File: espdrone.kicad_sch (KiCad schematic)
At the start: 46 parts, among them U15 TPD2EUSB30A, U3 W25Q128JVP, U7 GT-USB-7079C, Y1 Crystal_GND24

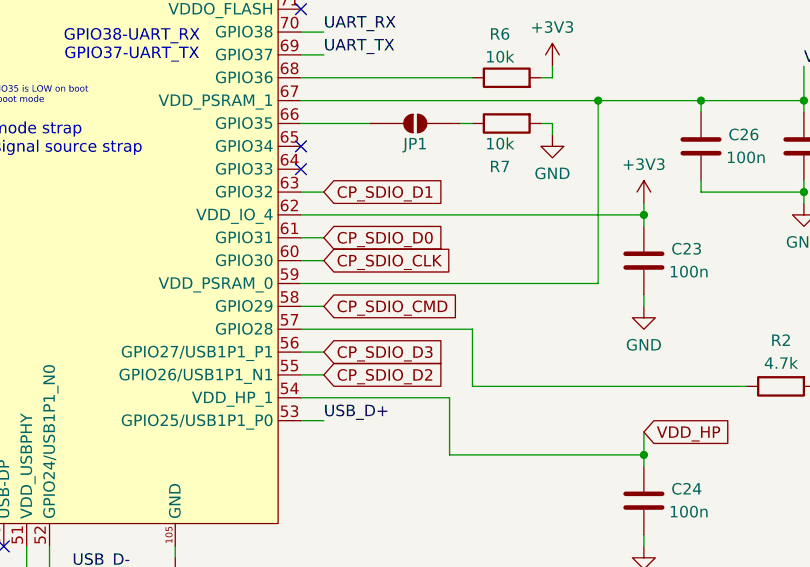
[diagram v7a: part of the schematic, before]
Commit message: Add some FC vias
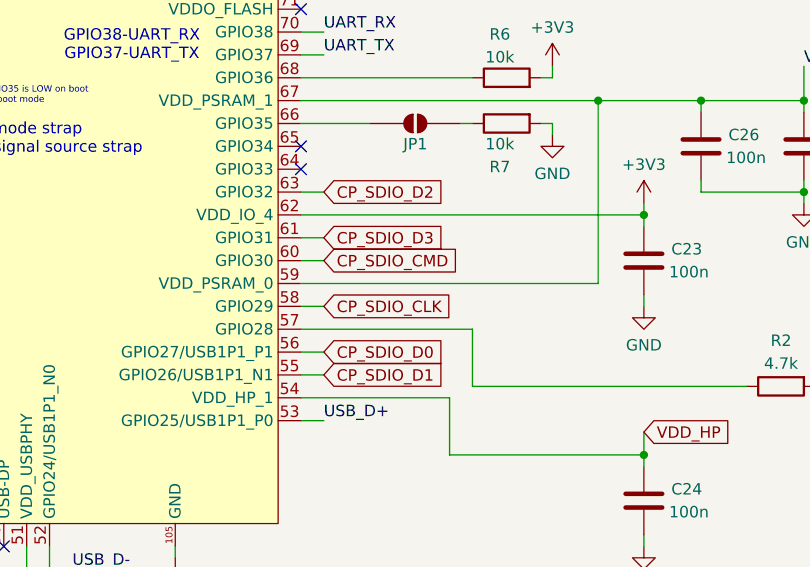
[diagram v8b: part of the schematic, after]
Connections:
- net CP_SDIO_CLK: now also U1.58 (GPIO29); no longer U1.60 (GPIO30)
- net CP_SDIO_CMD: now also U1.60 (GPIO30); no longer U1.58 (GPIO29)
- net CP_SDIO_D0: now also U1.56 (GPIO27/USB1P1_P1); no longer U1.61 (GPIO31)
- net CP_SDIO_D1: now also U1.55 (GPIO26/USB1P1_N1); no longer U1.63 (GPIO32)
- net CP_SDIO_D2: now also U1.63 (GPIO32); no longer U1.55 (GPIO26/USB1P1_N1)
- net CP_SDIO_D3: now also U1.61 (GPIO31); no longer U1.56 (GPIO27/USB1P1_P1)
